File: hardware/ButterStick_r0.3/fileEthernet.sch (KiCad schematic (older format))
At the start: 54 parts, among them CON1 JD1_0001NL, U10 XCL206B123CR-G, U11 KSZ9031, U13 SN74LVC1T45, U14 SN74LVC1T45, Y1 25Mhz

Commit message: hw.r0_3: Experiment with buses
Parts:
- C25, C26, C27, C28, C29, C30, C31, C32, C33, C34, C35, C36, C37, C5, C72: footprint pkl_dipol:C_0402 -> Capacitor_SMD:C_0402_1005Metric
- C40, C41, C55: footprint pkl_dipol:C_0603 -> Capacitor_SMD:C_0603_1608Metric
- R10, R11, R12, R13, R14, R15, R20, R21, R24, R48, R49, R50, R51, R52, R55, R64, R65, R67, R68, R69, R7, R70, R71, R72, R77, R8, R9: footprint pkl_dipol:R_0402 -> Resistor_SMD:R_0402_1005Metric
- R19: footprint pkl_dipol:R_0603 -> Resistor_SMD:R_0402_1005Metric

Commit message: hw.r0_3: cleanup and additions
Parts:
- removed R10, R11, R12, R13, R14, R7, R8, R9: 1k5, Resistor_SMD:R_0402_1005Metric, symbol Device:R
- removed U10: XCL206B123CR-G, gkl_housings_dfn:CL-2025, symbol gkl_pmic:XCL206
- removed U13, U14: SN74LVC1T45, TO_SOT_Packages_SMD:SOT-666, symbol gkl_misc:SN74LVC1T45
- added CON2: JD1_0001NL, gkl_conn:MAGJACK, symbol gkl_misc:JD1_0001NL
- added L5: 600R, pkl_dipol:L_0603, symbol Device:Ferrite_Bead_Small
- added Q7, Q8: PMBT3904MB, Package_TO_SOT_SMD:SOT-883, symbol gkl_misc:PMBT3904MB
- added R34, R60, R78, R79, R80, R81, R82, R83: 1k5, Resistor_SMD:R_0402_1005Metric, symbol Device:R
- added R84, R85: 220R, Resistor_SMD:R_0402_1005Metric, symbol Device:R
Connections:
- net labels added: MDC, MDIO, RESET, TX0, TX1, TX2, TX3, {RGMII}
- wire segments 223 -> 234
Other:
- moved on the sheet: C25, C26, C27, C28, C29, C30, C31, C32, C33, C34, C35, C36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

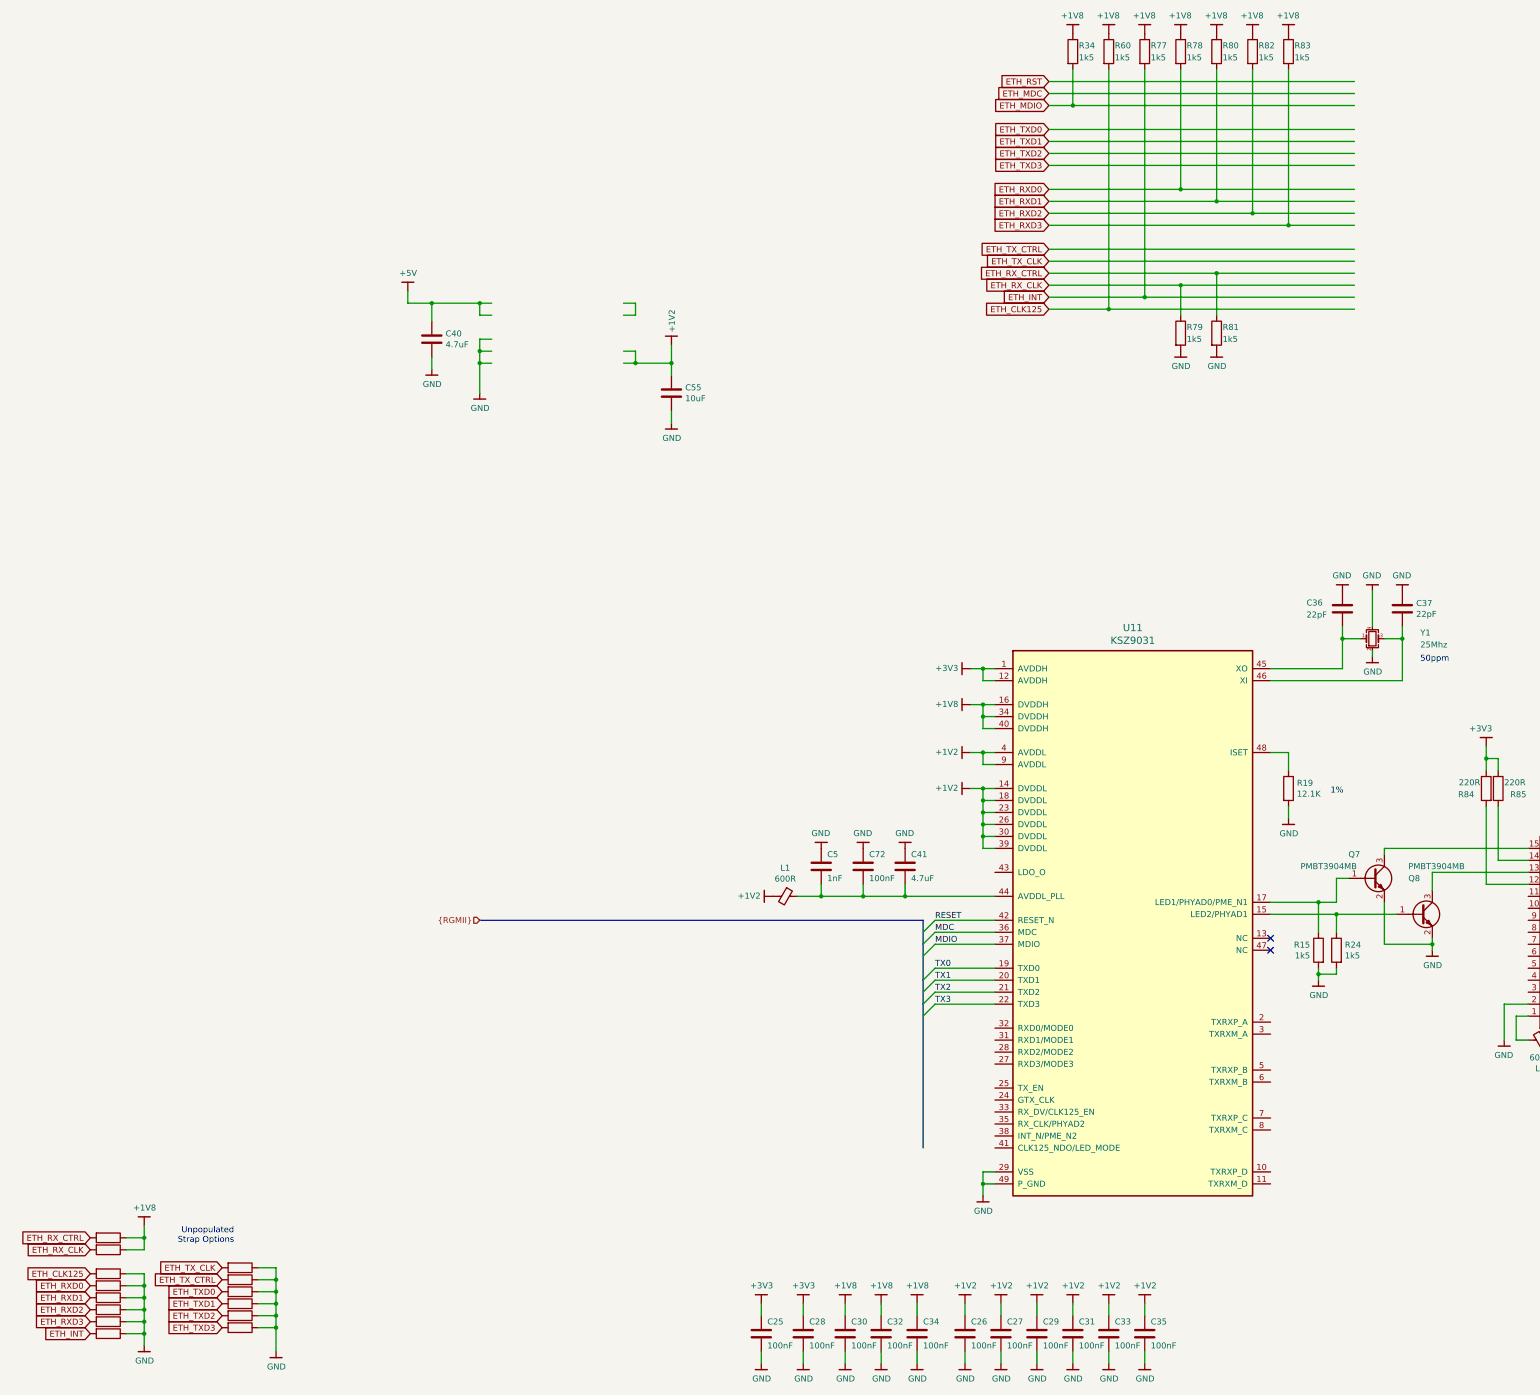
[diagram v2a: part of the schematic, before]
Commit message: hw.r0_3: Update schematics with 85F-5G symbol
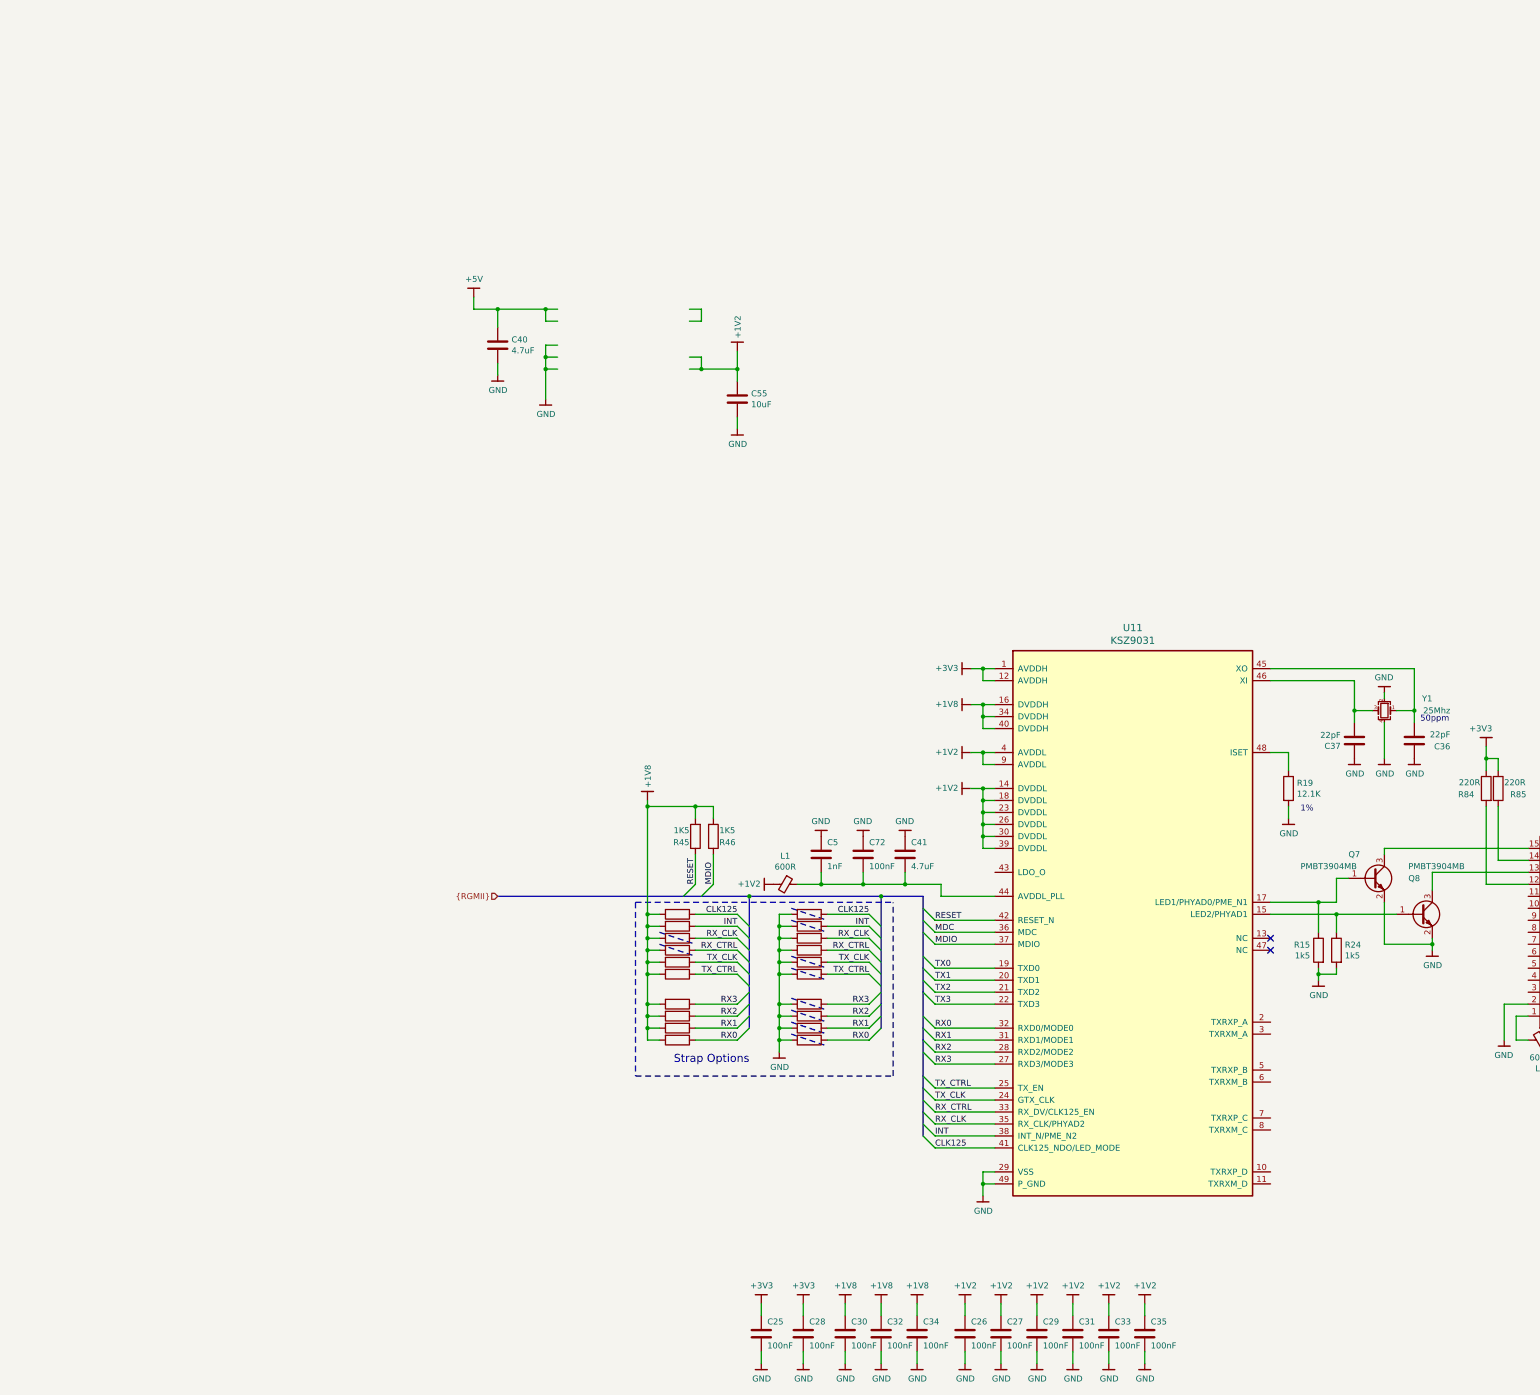
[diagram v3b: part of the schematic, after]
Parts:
- removed R60, R77, R78, R79, R80, R81, R82, R83: 1k5, Resistor_SMD:R_0402_1005Metric, symbol Device:R
- removed R64, R65, R67, R68, R69, R70, R71, R72: DNP, Resistor_SMD:R_0402_1005Metric, symbol Device:R
- added R36, R37, R38, R39, R40, R41, R42, R43, R44, R53, R54, R56, R57: DNP, Resistor_SMD:R_0402_1005Metric, symbol Device:R
- added R45, R46: 1K5, Resistor_SMD:R_0402_1005Metric, symbol Device:R
- R34: value 1k5 -> DNP; PN RC0402FR-071K5L -> DNP; SN-DK 311-1.50KLRCT-ND -> (none)
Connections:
- net labels added: CLK125, INT, RX0, RX1, RX2, RX3, RX_CLK, RX_CTRL, TX_CLK, TX_CTRL
- net labels removed: ETH_CLK125, ETH_INT, ETH_MDC, ETH_MDIO, ETH_RST, ETH_RXD0, ETH_RXD1, ETH_RXD2, ETH_RXD3, ETH_RX_CLK, ETH_RX_CTRL, ETH_TXD0, ETH_TXD1, ETH_TXD2, ETH_TXD3, ETH_TX_CLK, ETH_TX_CTRL
- wire segments 234 -> 250
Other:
- note added: "Strap Options"
- note removed: "Unpopulated \nStrap Options"
- moved on the sheet: C36, C37, C40, C41, C5, C55, C72, L1, Y1

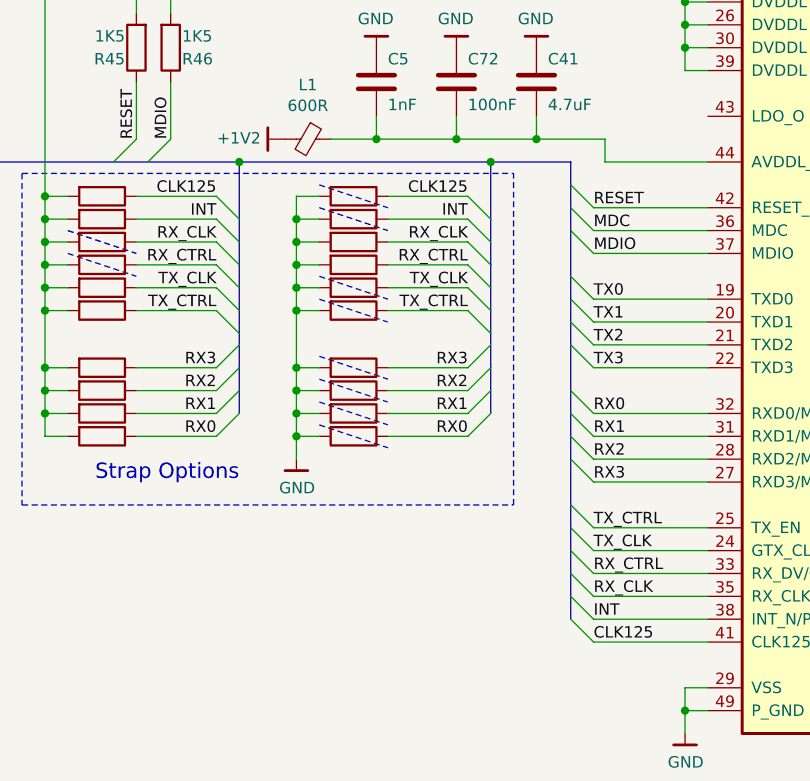
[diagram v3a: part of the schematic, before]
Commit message: hw.r0_3: Start pin assignments for DDR3
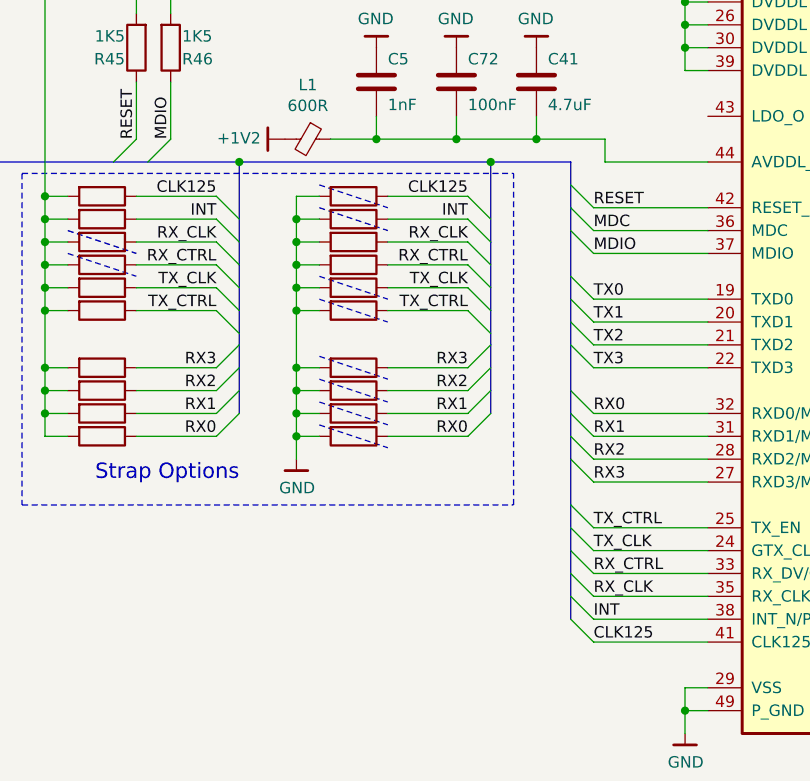
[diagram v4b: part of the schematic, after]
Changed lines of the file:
@@
 $Descr A4 11693 8268
 encoding utf-8
-Sheet 17 18
+Sheet 7 20
 Title "ButterStick"
 Date "2019-06-14"
@@
 	3300 3600 4400 3600
 Wire Bus Line
-	3300 3950 3300 4150
-Wire Bus Line
-	3300 4150 3300 4350
-Wire Bus Line
-	3300 4350 3300 4500
+	3300 3950 3300 4050
+Wire Bus Line
+	3300 4050 3300 4250
+Wire Bus Line
+	3300 4250 3300 4400
+Wire Bus Line
+	3300 4400 3300 4500
 Wire Bus Line
 	3300 4500 3300 4700
 Wire Bus Line
-	4400 3600 4400 3850
+	4400 3600 4400 3950
 Wire Bus Line
 	4400 3600 4750 3600
 Wire Bus Line
-	4400 3850 4400 4050
-Wire Bus Line
-	4400 4050 4400 4250
-Wire Bus Line
-	4400 4250 4400 4350
-Wire Bus Line
-	4400 4350 4400 4500
-Wire Bus Line
-	4400 4500 4400 4700
-Wire Bus Line
-	4750 3600 4750 3700
-Wire Bus Line
-	4750 3700 4750 3900
-Wire Bus Line
-	4750 3900 4750 4200
-Wire Bus Line
-	4750 4200 4750 4400
-Wire Bus Line
-	4750 4400 4750 4700
-Wire Bus Line
-	4750 4700 4750 4800
-Wire Bus Line
-	4750 4800 4750 5100
-Wire Bus Line
-	4750 5100 4750 5200
-Wire Bus Line
-	4750 5200 4750 5400
-Wire Bus Line
-	4750 5400 4750 5600
+	4400 3950 4400 4150
+Wire Bus Line
+	4400 4150 4400 4250
+Wire Bus Line
+	4400 4250 4400 4400
+Wire Bus Line
+	4400 4400 4400 4600
+Wire Bus Line
+	4400 4600 4400 4700
+Wire Bus Line
+	4750 3600 4750 3800
+Wire Bus Line
+	4750 3800 4750 4100
+Wire Bus Line
+	4750 4100 4750 4300
+Wire Bus Line
+	4750 4300 4750 4600
+Wire Bus Line
+	4750 4600 4750 4700
+Wire Bus Line
+	4750 4700 4750 4900
+Wire Bus Line
+	4750 4900 4750 5100
+Wire Bus Line
+	4750 5100 4750 5300
+Wire Bus Line
+	4750 5300 4750 5500
+Wire Bus Line
+	4750 5500 4750 5600
 Wire Notes Line
 	2350 3650 2350 5100
